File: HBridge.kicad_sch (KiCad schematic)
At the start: 12 parts, among them Q1 STD5N20L, Q2 STD5N20L, Q3 STD5N20L, Q4 STD5N20L, U1 IRS2005M, U4 IRS2005M

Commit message: Updated references after merging
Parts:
- renumbered C7 to C10, C6 to C9, D2 to D3, D3 to D4, R8 to R19, R9 to R20, U1 to U4, U4 to U5
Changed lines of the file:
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@@
 		(on_board yes)
 		(dnp no)
-		(property "Reference" "C7"
+		(property "Reference" "C10"
 			(at 180.34 85.0899 0)
 			(effects
@@
 			(project "FES_Hardware"
 				(path "/225cfa82-97e7-4320-90e1-4d94ef39f9f2/743d8807-83c0-4706-a128-4bbbd94e26d6"
-					(reference "C7")
+					(reference "C10")
 					(unit 1)
 				)
@@
 		(on_board yes)
 		(dnp no)
-		(property "Reference" "U4"
+		(property "Reference" "U5"
 			(at 201.676 82.804 0)
 			(effects
@@
 			(project "FES_Hardware"
 				(path "/225cfa82-97e7-4320-90e1-4d94ef39f9f2/743d8807-83c0-4706-a128-4bbbd94e26d6"
-					(reference "U4")
+					(reference "U5")
 					(unit 1)
 				)
@@
 		(dnp no)
 		(fields_autoplaced yes)
-		(property "Reference" "D2"
+		(property "Reference" "D3"
 			(at 108.2675 71.12 0)
 			(effects
@@
 			(project ""
 				(path "/225cfa82-97e7-4320-90e1-4d94ef39f9f2/743d8807-83c0-4706-a128-4bbbd94e26d6"
-					(reference "D2")
+					(reference "D3")
 					(unit 1)
 				)
@@
 		(on_board yes)
 		(dnp no)
-		(property "Reference" "C6"
+		(property "Reference" "C9"
 			(at 119.38 85.0899 0)
 			(effects
@@
 			(project ""
 				(path "/225cfa82-97e7-4320-90e1-4d94ef39f9f2/743d8807-83c0-4706-a128-4bbbd94e26d6"
-					(reference "C6")
+					(reference "C9")
 					(unit 1)
 				)
@@
 		(on_board yes)
 		(dnp no)
-		(property "Reference" "U1"
+		(property "Reference" "U4"
 			(at 88.9 82.804 0)
 			(effects
@@
 			(project ""
 				(path "/225cfa82-97e7-4320-90e1-4d94ef39f9f2/743d8807-83c0-4706-a128-4bbbd94e26d6"
-					(reference "U1")
+					(reference "U4")
 					(unit 1)
 				)
@@
 		(dnp no)
 		(fields_autoplaced yes)
-		(property "Reference" "#PWR017"
+		(property "Reference" "#PWR018"
 			(at 92.71 77.47 0)
 			(effects
@@
 			(project ""
 				(path "/225cfa82-97e7-4320-90e1-4d94ef39f9f2/743d8807-83c0-4706-a128-4bbbd94e26d6"
-					(reference "#PWR017")
+					(reference "#PWR018")
 					(unit 1)
 				)
@@
 		(on_board yes)
 		(dnp no)
-		(property "Reference" "R8"
+		(property "Reference" "R19"
 			(at 131.826 101.854 90)
 			(effects
@@
 			(project "FES_Hardware"
 				(path "/225cfa82-97e7-4320-90e1-4d94ef39f9f2/743d8807-83c0-4706-a128-4bbbd94e26d6"
-					(reference "R8")
+					(reference "R19")
 					(unit 1)
 				)
@@
 		(dnp no)
 		(fields_autoplaced yes)
-		(property "Reference" "#PWR016"
+		(property "Reference" "#PWR021"
 			(at 196.85 119.38 0)
 			(effects
@@
 			(project "FES_Hardware"
 				(path "/225cfa82-97e7-4320-90e1-4d94ef39f9f2/743d8807-83c0-4706-a128-4bbbd94e26d6"
-					(reference "#PWR016")
+					(reference "#PWR021")
 					(unit 1)
 				)
@@
 		(on_board yes)
 		(dnp no)
-		(property "Reference" "D3"
+		(property "Reference" "D4"
 			(at 191.4525 71.12 0)
 			(effects
@@
 			(project "FES_Hardware"
 				(path "/225cfa82-97e7-4320-90e1-4d94ef39f9f2/743d8807-83c0-4706-a128-4bbbd94e26d6"
-					(reference "D3")
+					(reference "D4")
 					(unit 1)
 				)
@@
 		(dnp no)
 		(fields_autoplaced yes)
-		(property "Reference" "#PWR018"
+		(property "Reference" "#PWR022"
 			(at 205.74 77.47 0)
 			(effects
@@
 			(project "FES_Hardware"
 				(path "/225cfa82-97e7-4320-90e1-4d94ef39f9f2/743d8807-83c0-4706-a128-4bbbd94e26d6"
-					(reference "#PWR018")
+					(reference "#PWR022")
 					(unit 1)
 				)
@@
 		(dnp no)
 		(fields_autoplaced yes)
-		(property "Reference" "#PWR015"
+		(property "Reference" "#PWR020"
 			(at 149.86 127 0)
 			(effects
@@
 			(project ""
 				(path "/225cfa82-97e7-4320-90e1-4d94ef39f9f2/743d8807-83c0-4706-a128-4bbbd94e26d6"
-					(reference "#PWR015")
+					(reference "#PWR020")
 					(unit 1)
 				)
@@
 		(dnp no)
 		(fields_autoplaced yes)
-		(property "Reference" "#PWR013"
+		(property "Reference" "#PWR019"
 			(at 102.87 119.38 0)
 			(effects
@@
 			(project "FES_Hardware"
 				(path "/225cfa82-97e7-4320-90e1-4d94ef39f9f2/743d8807-83c0-4706-a128-4bbbd94e26d6"
-					(reference "#PWR013")
+					(reference "#PWR019")
 					(unit 1)
 				)
@@
 		(on_board yes)
 		(dnp no)
-		(property "Reference" "R9"
+		(property "Reference" "R20"
 			(at 165.7924 101.854 90)
 			(effects
@@
 			(project "FES_Hardware"
 				(path "/225cfa82-97e7-4320-90e1-4d94ef39f9f2/743d8807-83c0-4706-a128-4bbbd94e26d6"
-					(reference "R9")
-					(unit 1)
-				)
+					(reference "R20")
+					(unit 1)
+				)

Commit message: Updated footprints of passive elements to be 0805 Hand-Solder
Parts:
- C10, C9: footprint (none) -> Capacitor_SMD:C_0805_2012Metric_Pad1.18x1.45mm_HandSolder
- R19, R20: footprint (none) -> Resistor_SMD:R_0805_2012Metric_Pad1.20x1.40mm_HandSolder
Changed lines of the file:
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@@
 			)
 		)
-		(property "Footprint" ""
+		(property "Footprint" "Capacitor_SMD:C_0805_2012Metric_Pad1.18x1.45mm_HandSolder"
 			(at 185.1152 90.17 0)
 			(effects
@@
 			)
 		)
-		(property "Footprint" ""
+		(property "Footprint" "Capacitor_SMD:C_0805_2012Metric_Pad1.18x1.45mm_HandSolder"
 			(at 116.5352 90.17 0)
 			(effects
@@
 			)
 		)
-		(property "Footprint" ""
+		(property "Footprint" "Resistor_SMD:R_0805_2012Metric_Pad1.20x1.40mm_HandSolder"
 			(at 133.604 98.044 90)
 			(effects
@@
 			)
 		)
-		(property "Footprint" ""
+		(property "Footprint" "Resistor_SMD:R_0805_2012Metric_Pad1.20x1.40mm_HandSolder"
 			(at 167.5704 98.044 90)
 			(effects

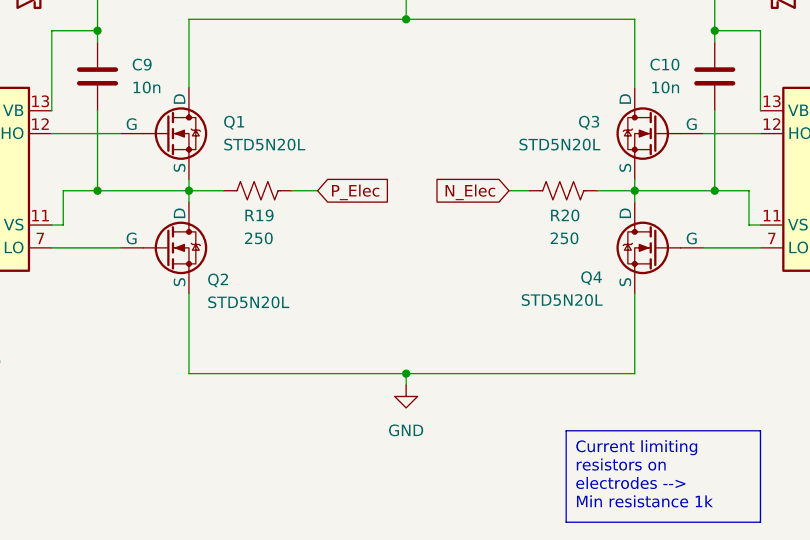
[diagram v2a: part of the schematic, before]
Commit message: added transformer and NMOS footprints
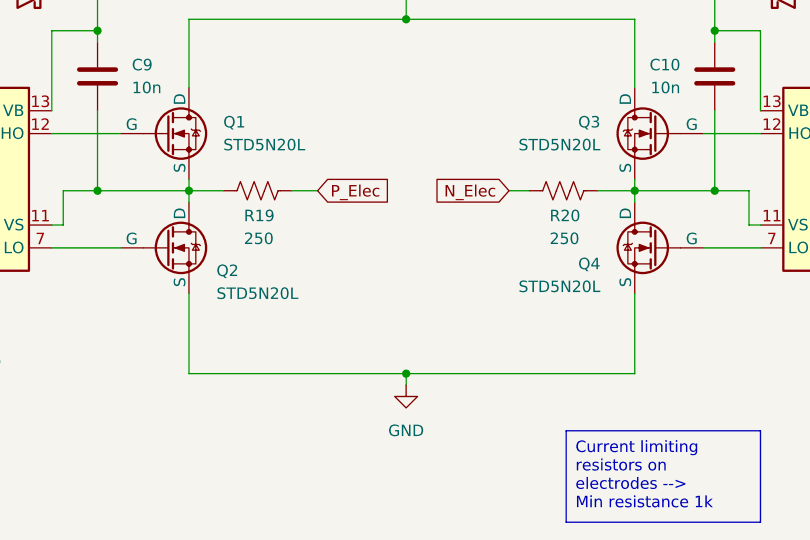
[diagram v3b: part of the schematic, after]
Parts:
- Q1, Q2, Q3, Q4: footprint (none) -> FES_Footprints:STD5N

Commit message: Hopefully finalized schematic with footprints
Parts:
- added J1: Screw_Terminal_01x02, Screw-Terminal-1x2:691137710002, symbol Connector:Screw_Terminal_01x02
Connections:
- net N_Elec: now also J1.1 (Pin_1)
- net P_Elec: now also J1.2 (Pin_2)

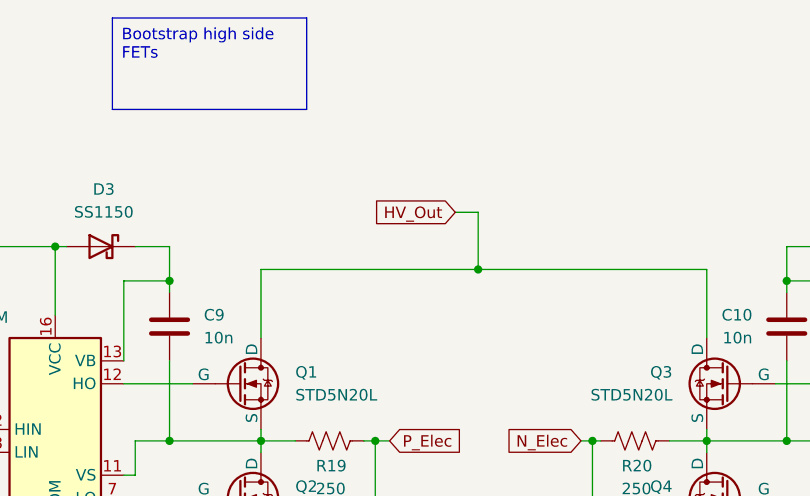
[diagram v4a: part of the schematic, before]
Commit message: tidied up PCB routing, renamed HV_OUT, changed MCU footprint/schematic
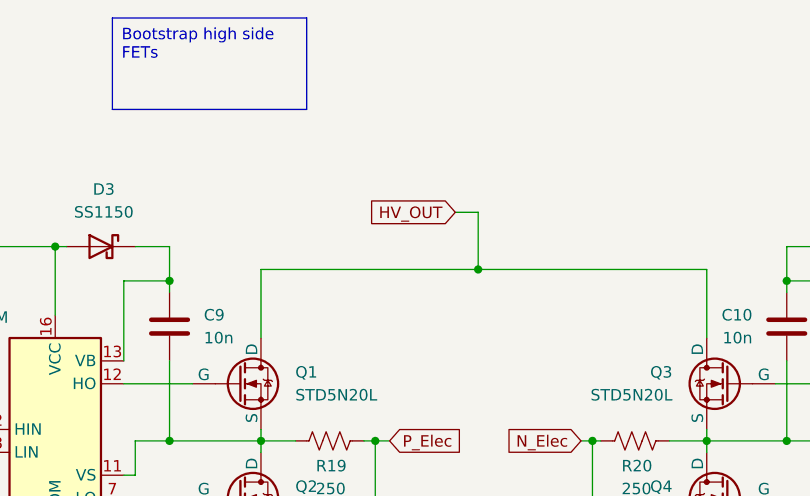
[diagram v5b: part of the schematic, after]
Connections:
- net HV_Out renamed HV_OUT
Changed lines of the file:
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@@
 		)
 	)
-	(global_label "HV_Out"
+	(global_label "HV_OUT"
 		(shape input)
 		(at 147.32 73.66 180)
@@
 		)
 		(property "Intersheetrefs" "${INTERSHEET_REFS}"
-			(at 137.7429 73.66 0)
+			(at 137.3195 73.66 0)
 			(effects
 				(font
